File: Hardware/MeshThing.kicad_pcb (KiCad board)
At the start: 2 copper layers, 25.7 x 27.8 mm, 28 parts, among them IC1 ATMEGA2564/1284/644RFR2, SW1 RST, U1 CONN_MICROSD, U2 XBEE, U3 XBEE

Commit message: More checks.
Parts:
- turned XTAL2 to 0 degrees
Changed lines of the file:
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@@
     (18 B.Paste user)
     (19 F.Paste user)
-    (20 B.SilkS user hide)
+    (20 B.SilkS user)
     (21 F.SilkS user)
     (22 B.Mask user)
@@
     (mod_text_size 1.5 1.5)
     (mod_text_width 0.15)
-    (pad_size 1 0.3)
+    (pad_size 0.8 0.8)
     (pad_drill 0)
     (pad_to_mask_clearance 0.2)
     (pad_to_paste_clearance_ratio -0.1)
     (aux_axis_origin 135.66 132.51)
-    (visible_elements FFFFFF7F)
+    (visible_elements FFFFF77F)
     (pcbplotparams
       (layerselection 284983297)
@@
       (xy -1.36398 2.0193)) (layer B.SilkS) (width 0.00254))
   )
-  (module _MT_TF32D-32768-Crystal (layer F.Cu)
-    (at 142.37 110.9 180)
-    (fp_text reference XTAL2 (at 1.25 0 270) (layer F.SilkS)
-      (effects (font (size 0.4 0.4) (thickness 0.1)))
-    )
-    (fp_text value 32kHz (at -1.25 0 270) (layer F.SilkS)
-      (effects (font (size 0.5 0.5) (thickness 0.125)))
-    )
-    (fp_line (start -0.625 -0.75) (end 0.625 -0.75) (layer F.SilkS) (width 0.15))
-    (fp_line (start -0.625 0.75) (end 0.625 0.75) (layer F.SilkS) (width 0.15))
-    (pad 1 smd rect (at 1.25 0 180) (size 1 1.8)
-      (layers F.Cu F.Paste F.Mask)
-      (net 15 N-0000027)
-    )
-    (pad 2 smd rect (at -1.25 0 180) (size 1 1.8)
-      (layers F.Cu F.Paste F.Mask)
-      (net 16 N-0000028)
-    )
-  )
   (module _MT_LED-0603 (layer F.Cu)
     (at 156.15 124.34 90)
@@
       (layers F.Cu F.Paste F.Mask)
       (net 31 N-0000056)
+    )
+  )
+  (module _MT_TF32D-32768-Crystal (layer F.Cu)
+    (at 142.37 110.9)
+    (fp_text reference XTAL2 (at -1.26 0 90) (layer F.SilkS)
+      (effects (font (size 0.4 0.4) (thickness 0.1)))
+    )
+    (fp_text value 32kHz (at 1.31 0.01 90) (layer F.SilkS)
+      (effects (font (size 0.5 0.5) (thickness 0.125)))
+    )
+    (fp_line (start -0.625 -0.75) (end 0.625 -0.75) (layer F.SilkS) (width 0.15))
+    (fp_line (start -0.625 0.75) (end 0.625 0.75) (layer F.SilkS) (width 0.15))
+    (pad 2 smd rect (at 1.25 0) (size 1 1.8)
+      (layers F.Cu F.Paste F.Mask)
+      (net 16 N-0000028)
+    )
+    (pad 1 smd rect (at -1.25 0) (size 1 1.8)
+      (layers F.Cu F.Paste F.Mask)
+      (net 15 N-0000027)
     )
   )
@@
   (segment (start 156.61 126.022) (end 157.53 125.102) (width 0.2032) (layer F.Cu) (net 14))
   (segment (start 141.66 109.262) (end 141.66 109.46) (width 0.2032) (layer F.Cu) (net 15))
+  (segment (start 143.35068 113.74) (end 142.77 113.74) (width 0.2032) (layer F.Cu) (net 15))
+  (segment (start 142.77 113.74) (end 141.12 112.09) (width 0.2032) (layer F.Cu) (net 15))
   (segment (start 141.12 110) (end 141.12 110.9) (width 0.2032) (layer F.Cu) (net 15))
   (segment (start 141.66 109.46) (end 141.12 110) (width 0.2032) (layer F.Cu) (net 15))
-  (segment (start 143.35068 113.74) (end 142.77 113.74) (width 0.2032) (layer F.Cu) (net 15))
-  (segment (start 142.77 113.74) (end 141.12 112.09) (width 0.2032) (layer F.Cu) (net 15))
   (segment (start 141.12 112.09) (end 141.12 110.9) (width 0.2032) (layer F.Cu) (net 15))
+  (segment (start 143.62 109.92) (end 143.62 110.9) (width 0.2032) (layer F.Cu) (net 16))
+  (segment (start 143.62 111.81055) (end 143.62 110.9) (width 0.2032) (layer F.Cu) (net 16))
   (segment (start 143.21 109.262) (end 143.21 109.51) (width 0.2032) (layer F.Cu) (net 16))
-  (segment (start 143.62 109.92) (end 143.62 110.9) (width 0.2032) (layer F.Cu) (net 16))
   (segment (start 143.21 109.51) (end 143.62 109.92) (width 0.2032) (layer F.Cu) (net 16))
+  (segment (start 144.05 112.24055) (end 143.62 111.81055) (width 0.2032) (layer F.Cu) (net 16))
   (segment (start 144.05 113.04068) (end 144.05 112.24055) (width 0.2032) (layer F.Cu) (net 16))
-  (segment (start 143.62 111.81055) (end 143.62 110.9) (width 0.2032) (layer F.Cu) (net 16))
-  (segment (start 144.05 112.24055) (end 143.62 111.81055) (width 0.2032) (layer F.Cu) (net 16))
   (segment (start 150.24932 116.74) (end 153.332 116.74) (width 0.2032) (layer F.Cu) (net 27))
   (segment (start 153.332 116.74) (end 153.6 116.472) (width 0.2032) (layer F.Cu) (net 27))

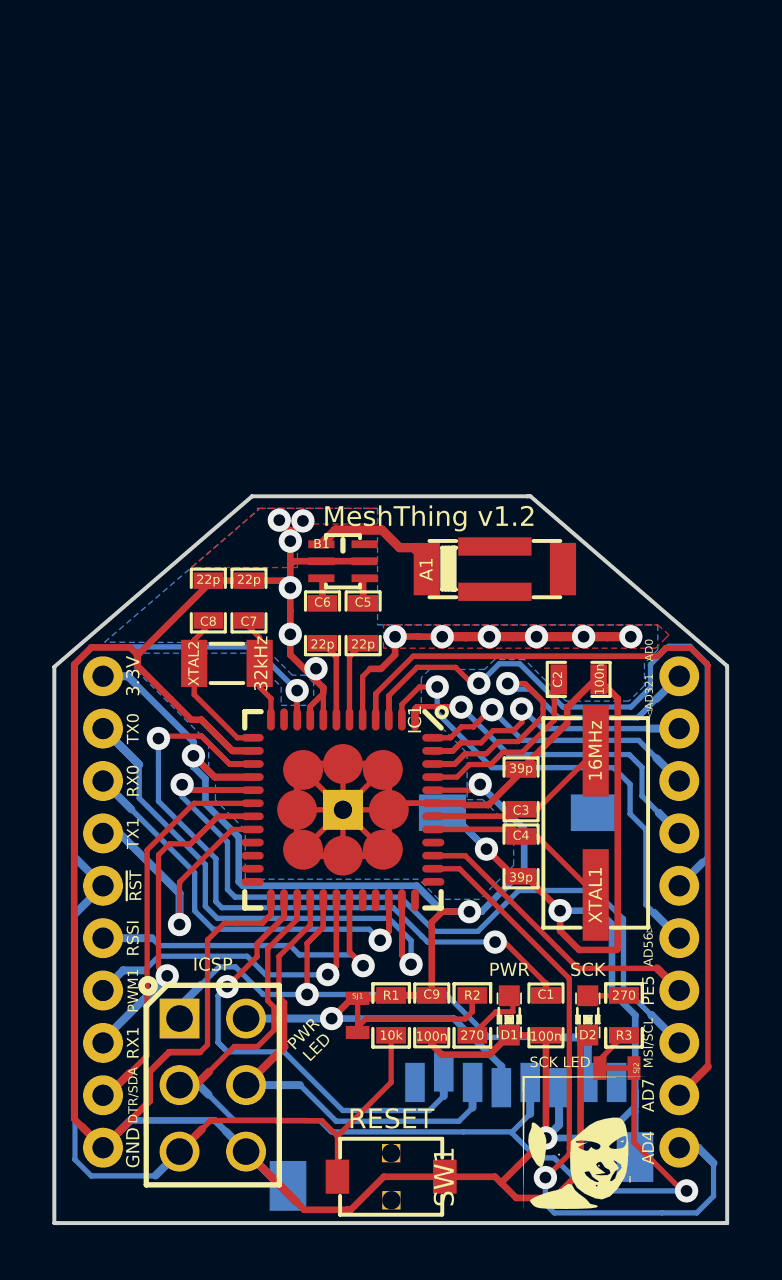
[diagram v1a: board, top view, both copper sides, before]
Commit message: Fiducials added, refining positions.
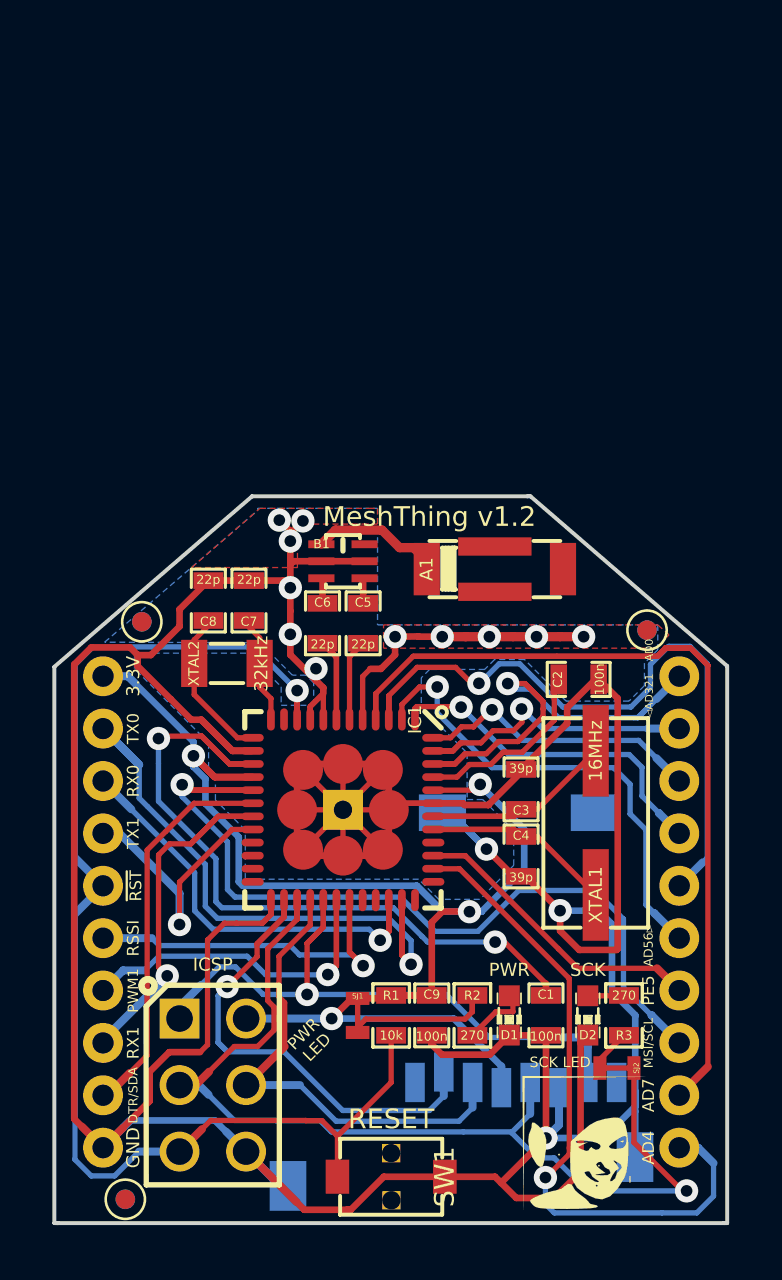
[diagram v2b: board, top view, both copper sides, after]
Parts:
- added _MT_Fiducial: VAL**, _MT_Fiducial, F.Cu at (139.1, 109.3)
- added _MT_Fiducial: VAL**, _MT_Fiducial, F.Cu at (138.5, 131.4)
- added _MT_Fiducial: VAL**, _MT_Fiducial, F.Cu at (158.4, 109.6)
- U1: footprint _MT_microSD_3M_290805 -> _MT_microSD_3M_290805-A
- moved U1 3.52 mm to (151.5, 124.0)
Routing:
- net GND: track 228.3 -> 226.8 mm, vias 15 -> 14

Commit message: v1.2 Production.
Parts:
- renumbered _MT_Fiducial to F1, _MT_Fiducial to F2, _MT_Fiducial to F3
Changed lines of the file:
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@@
     (links 87)
     (no_connects 0)
-    (area 135.704999 104.444999 161.545001 132.345001)
+    (area 134.250134 98.8424 163.059866 133.9482)
     (thickness 1.6)
     (drawings 16)
@@
   )
   (layers
-    (15 F.Cu signal)
-    (0 B.Cu signal)
-    (16 B.Adhes user)
-    (17 F.Adhes user)
-    (18 B.Paste user)
-    (19 F.Paste user)
-    (20 B.SilkS user)
+    (15 F.Cu signal hide)
+    (0 B.Cu signal hide)
+    (16 B.Adhes user hide)
+    (17 F.Adhes user hide)
+    (18 B.Paste user hide)
+    (19 F.Paste user hide)
+    (20 B.SilkS user hide)
     (21 F.SilkS user)
-    (22 B.Mask user)
-    (23 F.Mask user)
-    (24 Dwgs.User user)
-    (25 Cmts.User user)
-    (26 Eco1.User user)
-    (27 Eco2.User user)
+    (22 B.Mask user hide)
+    (23 F.Mask user hide)
+    (24 Dwgs.User user hide)
+    (25 Cmts.User user hide)
+    (26 Eco1.User user hide)
+    (27 Eco2.User user hide)
     (28 Edge.Cuts user)
   )
@@
     (pad_to_mask_clearance 0.2)
     (pad_to_paste_clearance_ratio -0.1)
-    (aux_axis_origin 135.66 132.51)
-    (visible_elements FFFFFF7F)
+    (aux_axis_origin 135.68 132.37)
+    (visible_elements FFFF5321)
     (pcbplotparams
       (layerselection 284983297)
@@
       (drillshape 0)
       (scaleselection 1)
-      (outputdirectory Gerbers/))
+      (outputdirectory /home/bob/Tmp/))
   )
   (net 0 "")
@@
       (effects (font (size 0.35 0.35) (thickness 0.075)))
     )
-    (fp_text user ◅AD321 (at 9.85 0.75 90) (layer F.SilkS)
-      (effects (font (size 0.3 0.3) (thickness 0.075)))
-    )
-    (fp_text user AD0 (at 9.85 -1 90) (layer F.SilkS)
+    (fp_text user ◅AD3210 (at 9.85 0.7 90) (layer F.SilkS)
       (effects (font (size 0.3 0.3) (thickness 0.075)))
     )
@@
   (module _MT_CSM-3X-Crystal (layer F.Cu)
     (at 156.45 116.99 90)
+    (attr smd)
     (fp_text reference XTAL1 (at -2.75 0 90) (layer F.SilkS)
       (effects (font (size 0.5 0.5) (thickness 0.125)))
@@
   (module _MT_XBee_Board_BackLablesOnly (layer B.Cu)
     (at 148.64 111.39)
+    (attr smd)
     (fp_text reference U3 (at -6.35 -7.62 90) (layer B.SilkS) hide
       (effects (font (thickness 0.3048)) (justify mirror))
@@
   (module LOGO (layer F.Cu)
     (at 155.94 129.19)
+    (attr smd)
     (fp_text reference G*** (at 0 3.302) (layer F.SilkS) hide
       (effects (font (thickness 0.3048)))
@@
   (module LOGO (layer B.Cu)
     (at 146.82 108.68)
+    (attr smd)
     (fp_text reference G*** (at 0 -2.38506) (layer B.SilkS) hide
       (effects (font (size 0.2032 0.2032) (thickness 0.04064)) (justify mirror))
@@
   (module _MT_TC007-TactileSwitch (layer F.Cu)
     (at 148.64 130.5 180)
+    (attr smd)
     (fp_text reference SW1 (at -2.04 0 270) (layer F.SilkS)
       (effects (font (size 0.75 0.75) (thickness 0.15)))
@@
     (pad "" thru_hole rect (at -0.01 -0.9 180) (size 0.7 0.7) (drill 0.7)
       (layers *.Cu *.Mask F.SilkS)
-    )
-  )
-  (module _MT_SMTJumper (layer F.Cu)
-    (at 147.36 124.34 270)
-    (attr smd)
-    (fp_text reference SJ1 (at -0.74 0 360) (layer F.SilkS)
-      (effects (font (size 0.2 0.2) (thickness 0.05)))
-    )
-    (fp_text value SMTJPR (at 0 0 270) (layer F.SilkS) hide
-      (effects (font (size 0.508 0.4572) (thickness 0.1143)))
-    )
-    (pad 1 smd rect (at -0.65 0 270) (size 0.5 0.9)
-      (layers F.Cu F.Mask)
-      (net 1 +3.3V)
-      (solder_mask_margin 0.01)
-    )
-    (pad 2 smd rect (at 0.65 0 270) (size 0.5 0.9)
-      (layers F.Cu F.Mask)
-      (net 8 N-0000015)
-      (solder_mask_margin 0.01)
-    )
-    (pad 3 smd rect (at 0 0 270) (size 1.5 0.2032)
-      (layers F.Cu F.Mask)
-      (solder_mask_margin 0.01)
-    )
-    (model smd\resistors\R0603.wrl
-      (at (xyz 0 0 0.001))
-      (scale (xyz 0.5 0.5 0.5))
-      (rotate (xyz 0 0 0))
-    )
-  )
-  (module _MT_SMTJumper (layer F.Cu)
-    (at 157.26 126.35 180)
-    (attr smd)
-    (fp_text reference SJ2 (at -0.74 0 270) (layer F.SilkS)
-      (effects (font (size 0.2 0.2) (thickness 0.05)))
-    )
-    (fp_text value SMTJPR (at 0 0 180) (layer F.SilkS) hide
-      (effects (font (size 0.508 0.4572) (thickness 0.1143)))
-    )
-    (pad 1 smd rect (at -0.65 0 180) (size 0.5 0.9)
-      (layers F.Cu F.Mask)
-      (net 51 SCK)
-      (solder_mask_margin 0.01)
-    )
-    (pad 2 smd rect (at 0.65 0 180) (size 0.5 0.9)
-      (layers F.Cu F.Mask)
-      (net 14 N-0000026)
-      (solder_mask_margin 0.01)
-    )
-    (pad 3 smd rect (at 0 0 180) (size 1.5 0.2032)
-      (layers F.Cu F.Mask)
-      (solder_mask_margin 0.01)
-    )
-    (model smd\resistors\R0603.wrl
-      (at (xyz 0 0 0.001))
-      (scale (xyz 0.5 0.5 0.5))
-      (rotate (xyz 0 0 0))
     )
   )
@@
   (module Johanson-2450AT42B100-PadsOnly (layer F.Cu)
     (at 152.6 107.3)
+    (attr smd)
     (fp_text reference A1 (at -2.61 0 90) (layer F.SilkS)
       (effects (font (size 0.5 0.5) (thickness 0.125)))
@@
   (module _MT_Wuerth748421245-A (layer F.Cu)
     (at 146.8 107)
+    (attr smd)
     (fp_text reference B1 (at -0.82 -0.66) (layer F.SilkS)
       (effects (font (size 0.35 0.35) (thickness 0.0875)))
@@
   (module _MT_TF32D-32768-Crystal (layer F.Cu)
     (at 142.37 110.9)
+    (attr smd)
     (fp_text reference XTAL2 (at -1.26 0 90) (layer F.SilkS)
       (effects (font (size 0.4 0.4) (thickness 0.1)))
@@
     )
   )
+  (module _MT_SMTJumper (layer F.Cu)
+    (at 147.36 124.34 270)
+    (attr smd)
+    (fp_text reference SJ1 (at -0.74 0 360) (layer F.SilkS) hide
+      (effects (font (size 0.2 0.2) (thickness 0.05)))
+    )
+    (fp_text value SMTJPR (at 0 0 270) (layer F.SilkS) hide
+      (effects (font (size 0.508 0.4572) (thickness 0.1143)))
+    )
+    (pad 1 smd rect (at -0.65 0 270) (size 0.5 0.9)
+      (layers F.Cu F.Mask)
+      (net 1 +3.3V)
+      (solder_mask_margin 0.01)
+    )
+    (pad 2 smd rect (at 0.65 0 270) (size 0.5 0.9)
+      (layers F.Cu F.Mask)
+      (net 8 N-0000015)
+      (solder_mask_margin 0.01)
+    )
+    (pad 3 smd rect (at 0 0 270) (size 1.5 0.2032)
+      (layers F.Cu F.Mask)
+      (solder_mask_margin 0.01)
+    )
+    (model smd\resistors\R0603.wrl
+      (at (xyz 0 0 0.001))
+      (scale (xyz 0.5 0.5 0.5))
+      (rotate (xyz 0 0 0))
+    )
+  )
+  (module _MT_SMTJumper (layer F.Cu)
+    (at 157.26 126.35 180)
+    (attr smd)
+    (fp_text reference SJ2 (at -0.74 0 270) (layer F.SilkS) hide
+      (effects (font (size 0.2 0.2) (thickness 0.05)))
+    )
+    (fp_text value SMTJPR (at 0 0 180) (layer F.SilkS) hide
+      (effects (font (size 0.508 0.4572) (thickness 0.1143)))
+    )
+    (pad 1 smd rect (at -0.65 0 180) (size 0.5 0.9)
+      (layers F.Cu F.Mask)
+      (net 51 SCK)
+      (solder_mask_margin 0.01)
+    )
+    (pad 2 smd rect (at 0.65 0 180) (size 0.5 0.9)
+      (layers F.Cu F.Mask)
+      (net 14 N-0000026)
+      (solder_mask_margin 0.01)
+    )
+    (pad 3 smd rect (at 0 0 180) (size 1.5 0.2032)
+      (layers F.Cu F.Mask)
+      (solder_mask_margin 0.01)
+    )
+    (model smd\resistors\R0603.wrl
+      (at (xyz 0 0 0.001))
+      (scale (xyz 0.5 0.5 0.5))
+      (rotate (xyz 0 0 0))
+    )
+  )
   (module _MT_Fiducial (layer F.Cu)
-    (at 139.12 109.31)
-    (fp_text reference _MT_Fiducial (at 0.11 2.595) (layer F.SilkS) hide
-      (effects (font (size 1.5 1.5) (thickness 0.15)))
+    (at 158.41 109.63)
+    (attr smd)
+    (fp_text reference F2 (at 0 0) (layer F.SilkS)
+      (effects (font (size 1 1) (thickness 0.15)))
     )
     (fp_text value VAL** (at 0.205 -3.26) (layer F.SilkS) hide
@@
   (module _MT_Fiducial (layer F.Cu)
     (at 138.49 131.36)
-    (fp_text reference _MT_Fiducial (at 0.11 2.595) (layer F.SilkS) hide
-      (effects (font (size 1.5 1.5) (thickness 0.15)))
+    (attr smd)
+    (fp_text reference F3 (at 0 0) (layer F.SilkS)
+      (effects (font (size 1 1) (thickness 0.15)))
     )
     (fp_text value VAL** (at 0.205 -3.26) (layer F.SilkS) hide
@@
   )
   (module _MT_Fiducial (layer F.Cu)
-    (at 158.41 109.63)
-    (fp_text reference _MT_Fiducial (at 0.11 2.595) (layer F.SilkS) hide
-      (effects (font (size 1.5 1.5) (thickness 0.15)))
+    (at 139.12 109.31)
+    (attr smd)
+    (fp_text reference F1 (at 0 0) (layer F.SilkS)
+      (effects (font (size 1 1) (thickness 0.15)))
     )
     (fp_text value VAL** (at 0.205 -3.26) (layer F.SilkS) hide

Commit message: Initial v2.0 commit.
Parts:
- removed C9: 100n, _MT_SM0603_Capa
- removed D1, D2: LED, _MT_LED-0603
- removed the G*** at (155.9, 129.2)
- removed the G*** at (146.8, 108.7)
- removed H2: ICSP, _MT_pin_array_3x2
- removed R2, R3: 270, _MT_SM0603_Resistor
- removed SJ1, SJ2: SMTJPR, _MT_SMTJumper
- removed SW1: RST, _MT_TC007-TactileSwitch
- removed U1: CONN_MICROSD, _MT_microSD_3M_290805-A
- removed U2: XBEE, _MT_XBee_Board_STD_THPads
- removed U3: XBEE, _MT_XBee_Board_BackLablesOnly
- added G***: LOGO, _MT_OHW_LOGO:LOGO, F.Cu at (157.1, 90.5)
- added H1: ICSP, _MT_MC_Pretty:_MC_pin_pad_3x2, B.Cu at (146.0, 104.5)
- added P1: CONN34, _MT_MC_Pretty:_MC_CanFootprint-34Pin, F.Cu at (150.0, 100.0)
- added PrettyLady: PrettyLady, _MT_MC_Pretty:_MC_LOGO-PrettyLady, F.Cu at (142.9, 90.3)
- added S1: RFShield, _MT_MC_Pretty:_MT_MC_EMIShield-16.5x16.5, F.Cu at (150.0, 102.8)
- A1: value Antenna -> ANTENNA; footprint Johanson-2450AT42B100-PadsOnly -> _MT_MC_Pretty:_MT_IFA-2.4GHzPCBAntenna
- C1, C2, C5, C6, C7, C8: footprint _MT_SM0603_Capa -> SMD_Packages:SM0402_c
- C3, C4: value 39p -> 10p; footprint _MT_SM0603_Capa -> SMD_Packages:SM0402_c
- F1, F2, F3: value VAL** -> CONN_1; footprint _MT_Fiducial -> _MT_MC_Pretty:_MT_Fiducial
- R1: footprint _MT_SM0603_Resistor -> SMD_Packages:SM0402_r
- XTAL1: value 16MHz -> CRYSTAL_SMD-TSX3225; footprint _MT_CSM-3X-Crystal -> _MT_MC_Pretty:16MHz-3.2x2.5mm-TSX-3225
- XTAL2: footprint _MT_TF32D-32768-Crystal -> _MT_MC_Pretty:_MC_TF32D-32768-Crystal
- moved F3 43.0 mm to (158.5, 93.4)
- moved R1 29.3 mm to (156.6, 96.1), turned to 180 degrees
- moved C1 27.3 mm to (156.6, 97.1), turned to 0 degrees
- moved A1 16.9 mm to (150.0, 90.6)
- moved XTAL2 13.7 mm to (144.4, 97.3)
- moved C2 13.5 mm to (156.6, 98.0)
- moved C3 13.5 mm to (156.4, 102.5), turned to 0 degrees
- moved C7 12.8 mm to (145.5, 95.9), turned to 0 degrees
- moved C8 12.7 mm to (143.4, 95.9), turned to 180 degrees
- moved IC1 12.6 mm to (148.9, 104.0)
- moved XTAL1 12.2 mm to (156.0, 104.8), turned to 0 degrees
- moved C4 11.5 mm to (156.4, 107.1), turned to 180 degrees
- moved C6 11.1 mm to (148.4, 98.5)
- moved C5 11.0 mm to (149.3, 98.5)
- moved B1 10.6 mm to (148.9, 96.6)
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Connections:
- A1 pad 2: N-0000040 -> GND
- C3 pad 1: N-0000051 -> Net-(C3-Pad1)
- C4 pad 1: N-0000052 -> Net-(C4-Pad1)
- IC1 pad 11: N-0000049 -> PG1
- IC1 pad 21: N-0000048 -> PD4
- IC1 pad 22: N-0000047 -> PD5
- IC1 pad 23: N-0000046 -> PD6
- IC1 pad 24: N-0000044 -> PD7
- IC1 pad 32: N-0000021 -> PB6
- IC1 pad 33: N-0000045 -> PB7
- IC1 pad 36: N-0000022 -> PE2
- IC1 pad 37: N-0000020 -> PE3
- IC1 pad 40: N-0000050 -> PE7
- IC1 pad 41: N-0000052 -> Net-(C4-Pad1)
- IC1 pad 42: N-0000051 -> Net-(C3-Pad1)
- XTAL1 pad 1: N-0000052 -> Net-(C3-Pad1)
- XTAL1 pad 2: N-0000051 -> GND
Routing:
- net GND: track 226.8 -> 94.8 mm, vias 14 -> 13
- net PF7: track 45.6 -> 16.0 mm, vias 0 -> 1
- net Reset: track 49.1 -> 22.9 mm, vias 1 -> 2
- net SCK: track 39.6 -> 15.1 mm
- net SCL: track 33.1 -> 9.61 mm, vias 1 -> 0
- net PE4: track 25.6 -> 8.87 mm
- net TX0: track 24.8 -> 9.87 mm
- net PF6: track 26.3 -> 12.0 mm, vias 1 -> 0
- net PE7: track 0.00 -> 13.5 mm, vias 0 -> 1
- net MISO: track 25.1 -> 11.6 mm, vias 1 -> 0
- net Net-(C1-Pad1): track 28.0 -> 15.5 mm
- net PG1: track 0.00 -> 11.0 mm, vias 0 -> 1
- net N-0000052: track 10.7 -> 0.00 mm
- net N-0000051: track 10.7 -> 0.00 mm
- net RX0: track 17.3 -> 7.22 mm, vias 1 -> 0
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- added copper zone on Inner1.Cu, net +3.3V
- added copper zone on Inner2.Cu, net GND
- removed copper zone on F.Cu, net GND
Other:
- board size 25.7 x 27.8 mm -> 19.1 x 24.7 mm
- copper layers 2 -> 4
- net class 10mil added: clearance 0.2032, trace_width 0.254, via_dia 0.889, via_drill 0.635
- net class Default: trace_width 0.254 -> 0.2032
- board text added: "MeshThing v2.0 M9Design.co"
- board text added: "MeshThing v2.0 © M9Design.co 2013 Designed by Robert Powers"
- board text added: "OpenHardware Under TAPR OHL tapr.org/OHL"
- board text removed: "MeshThing v1.2"
- board text removed: "PWR"
- board text removed: "PWR LED"
- board text removed: "RESET"
- board text removed: "SCK"
- board text removed: "SCK LED"
- board text removed: "©BobPowers 2013 OpenHardware Under TAPR OHL tapr.org/OHL"
